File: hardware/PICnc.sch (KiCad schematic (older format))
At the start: 30 parts, among them P1 RPi GPIO, P2 STEP/DIR, P3 3.3v DIGITAL/ANALOG IO, P4 5v IO, P5 ICSP, P6 RPi GPIO, P7 5v RPi, P8 5v INP, U1 PIC32MX764F128H, U2 LP2985LV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

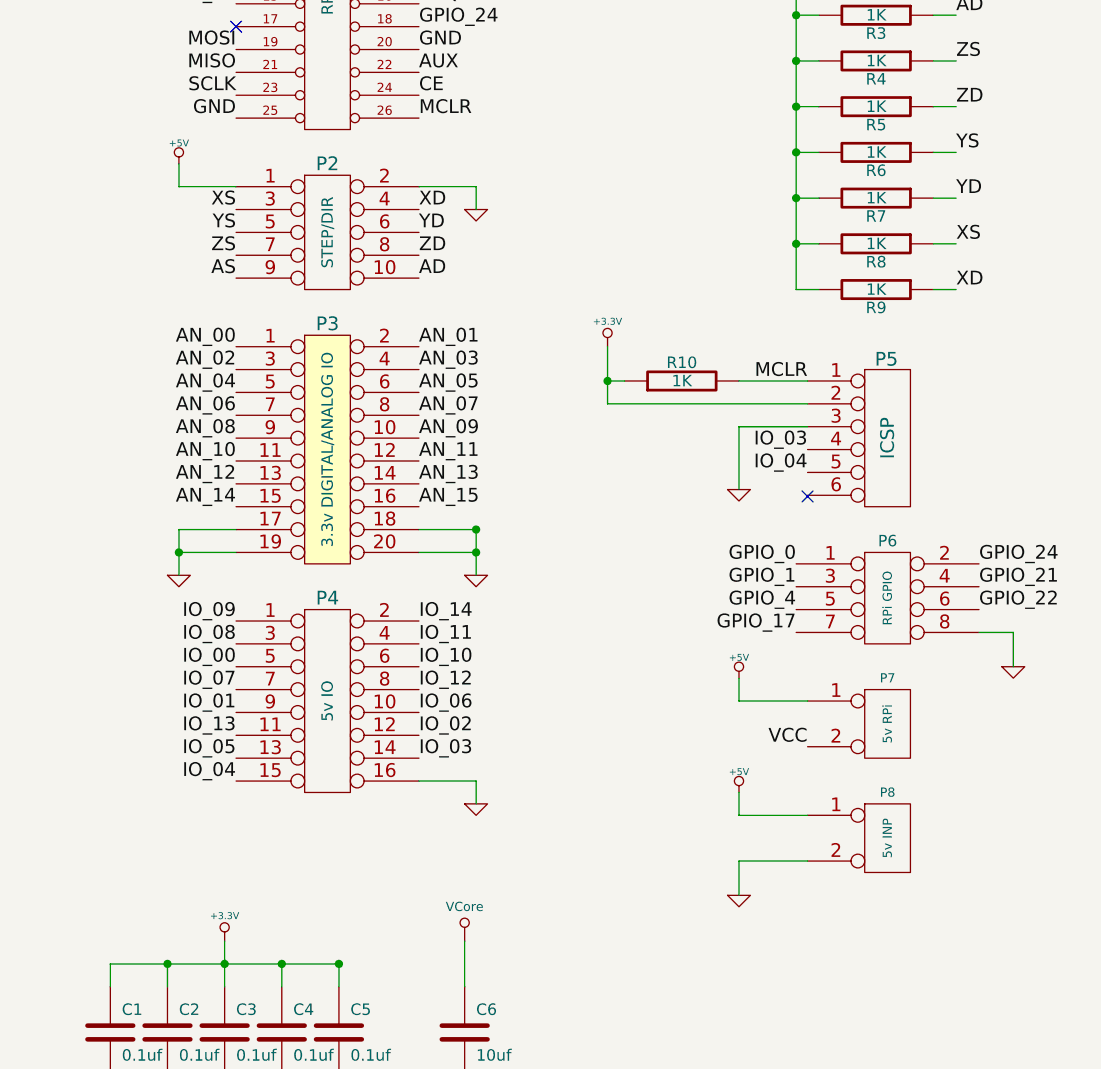
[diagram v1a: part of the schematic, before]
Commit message: fixed ICSP pinout
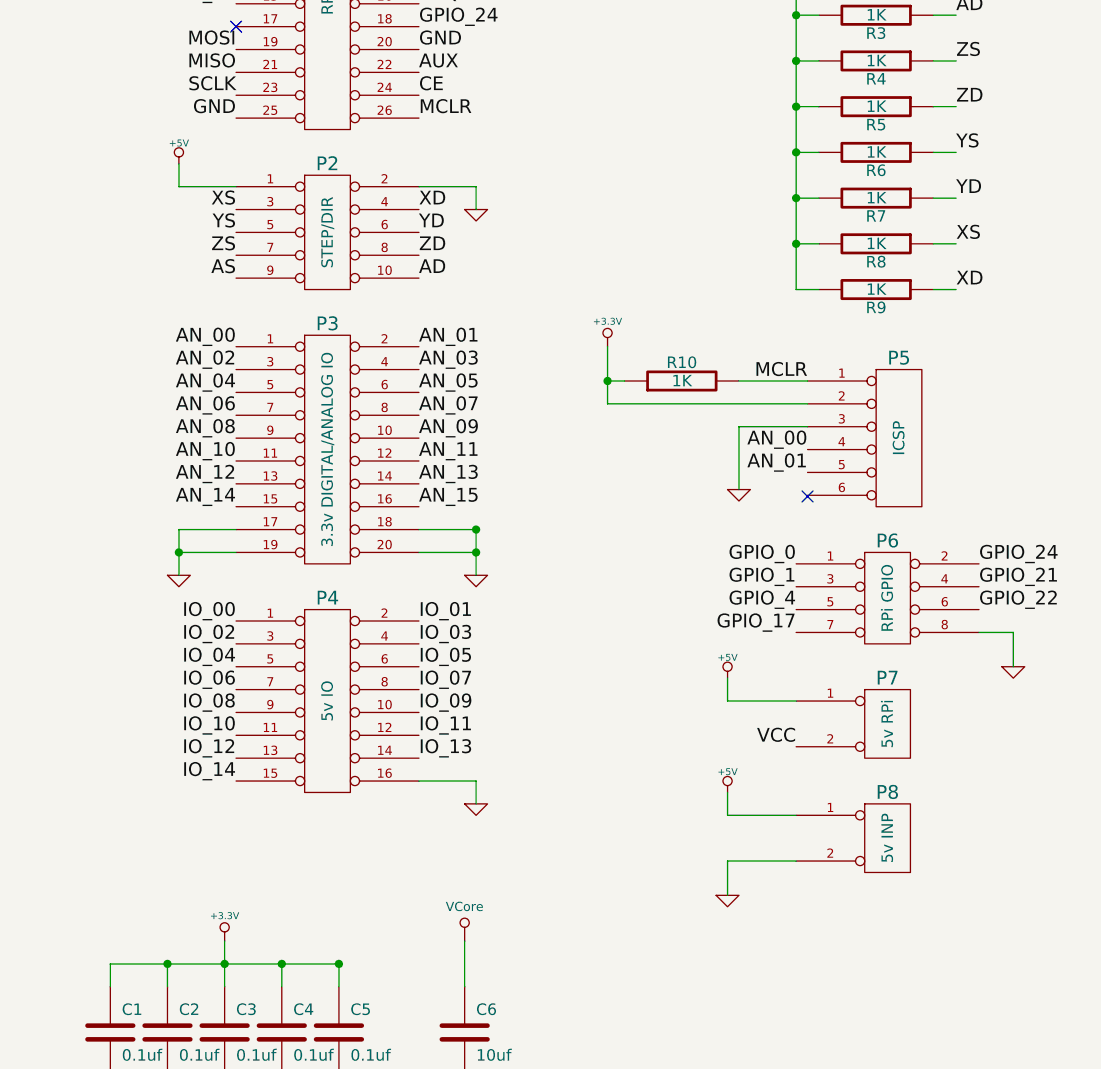
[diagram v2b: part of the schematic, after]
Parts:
- removed P2: STEP/DIR, symbol CONN_5X2
- removed P3: 3.3v DIGITAL/ANALOG IO, symbol CONN_10X2
- removed P4: 5v IO, symbol CONN_8X2
- removed P5: ICSP, symbol CONN_6
- removed P6: RPi GPIO, symbol CONN_4X2
- removed P7: 5v RPi, symbol CONN_2
- removed P8: 5v INP, symbol CONN_2
- added P2: STEP/DIR, symbol CON_5X2
- added P3: 3.3v DIGITAL/ANALOG IO, symbol CON_10X2
- added P4: 5v IO, symbol CON_8X2
- added P5: ICSP, symbol CON_6
- added P6: RPi GPIO, symbol CON_4X2
- added P7: 5v RPi, symbol CON_2
- added P8: 5v INP, symbol CON_2
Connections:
- net +3.3V: now also P5.2 (P2)
- net +5V: now also P2.1 (P1), P7.1 (P1), P8.1 (P1)
- net AD: now also P2.10 (P10)
- net AN_00: now also P3.1 (P1), P5.4 (P4)
- net AN_01: now also P3.2 (P2), P5.5 (P5)
- net AN_02: now also P3.3 (P3)
- net AN_03: now also P3.4 (P4)
- net AN_04: now also P3.5 (P5)
- net AN_05: now also P3.6 (P6)
- net AN_06: now also P3.7 (P7)
- net AN_07: now also P3.8 (P8)
- net AN_08: now also P3.9 (P9)
- net AN_09: now also P3.10 (P10)
- net AN_10: now also P3.11 (P11)
- net AN_11: now also P3.12 (P12)
- net AN_12: now also P3.13 (P13)
- net AN_13: now also P3.14 (P14)
- net AN_14: now also P3.15 (P15)
- net AN_15: now also P3.16 (P16)
- net AS: now also P2.9 (P9)
- net GND: now also P2.2 (P2), P3.17 (P17), P3.18 (P18), P3.19 (P19), P3.20 (P20), P4.16 (P16), P5.3 (P3), P6.8 (P8), P8.2 (P2)
- net GPIO_0: now also P6.1 (P1)
- net GPIO_1: now also P6.3 (P3)
- net GPIO_17: now also P6.7 (P7)
- net GPIO_21: now also P6.4 (P4)
- net GPIO_22: now also P6.6 (P6)
- net GPIO_24: now also P6.2 (P2)
- net GPIO_4: now also P6.5 (P5)
- net IO_00: now also P4.1 (P1)
- net IO_01: now also P4.2 (P2)
- net IO_02: now also P4.3 (P3)
- net IO_03: now also P4.4 (P4)
- net IO_04: now also P4.5 (P5)
- net IO_05: now also P4.6 (P6)
- net IO_06: now also P4.7 (P7)
- net IO_07: now also P4.8 (P8)
- net IO_08: now also P4.9 (P9)
- net IO_09: now also P4.10 (P10)
- net IO_10: now also P4.11 (P11)
- net IO_11: now also P4.12 (P12)
- net IO_12: now also P4.13 (P13)
- net IO_13: now also P4.14 (P14)
- net IO_14: now also P4.15 (P15)
- net MCLR: now also P5.1 (P1)
- net VCC: now also P7.2 (P2)
- net XD: now also P2.4 (P4)
- net XS: now also P2.3 (P3)
- net YD: now also P2.6 (P6)
- net YS: now also P2.5 (P5)
- net ZD: now also P2.8 (P8)
- net ZS: now also P2.7 (P7)
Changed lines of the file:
@@
-EESchema Schematic File Version 2  date Monday 18,February,2013 08:21:33 AM SGT
+EESchema Schematic File Version 2  date Monday 18,February,2013 12:46:50 PM SGT
 LIBS:power
 LIBS:device
@@
 Comment4 ""
 $EndDescr
-Wire Wire Line
-	9100 5850 9100 5700
-Wire Wire Line
-	9400 5500 9100 5500
-Wire Wire Line
-	9100 5500 9100 5400
+$Comp
+L CON_6 P5
+U 1 1 51218386
+P 9800 3850
+F 0 "P5" H 9800 4200 60  0000 C CNN
+F 1 "ICSP" V 9800 3850 50  0000 C CNN
+	1    9800 3850
+	1    0    0    -1
+$EndComp
+$Comp
+L CON_2 P8
+U 1 1 5121827C
+P 9750 5600
+F 0 "P8" H 9750 5800 60  0000 C CNN
+F 1 "5v INP" V 9750 5600 50  0000 C CNN
+	1    9750 5600
+	1    0    0    -1
+$EndComp
+$Comp
+L CON_2 P7
+U 1 1 51218259
+P 9750 5100
+F 0 "P7" H 9750 5300 60  0000 C CNN
+F 1 "5v RPi" V 9750 5100 50  0000 C CNN
+	1    9750 5100
+	1    0    0    -1
+$EndComp
+$Comp
+L CON_4X2 P6
+U 1 1 51218155
+P 9750 4550
+F 0 "P6" H 9750 4800 60  0000 C CNN
+F 1 "RPi GPIO" V 9750 4550 50  0000 C CNN
+	1    9750 4550
+	1    0    0    -1
+$EndComp
+$Comp
+L CON_5X2 P2
+U 1 1 51218129
+P 7300 2950
+F 0 "P2" H 7300 3250 60  0000 C CNN
+F 1 "STEP/DIR" V 7300 2950 50  0000 C CNN
+	1    7300 2950
+	1    0    0    -1
+$EndComp
+$Comp
+L CON_10X2 P3
+U 1 1 512180BA
+P 7300 3900
+F 0 "P3" H 7300 4450 60  0000 C CNN
+F 1 "3.3v DIGITAL/ANALOG IO" V 7300 3900 50  0000 C CNN
+	1    7300 3900
+	1    0    0    -1
+$EndComp
+$Comp
+L CON_8X2 P4
+U 1 1 51218077
+P 7300 5000
+F 0 "P4" H 7300 5450 60  0000 C CNN
+F 1 "5v IO" V 7300 5000 50  0000 C CNN
+	1    7300 5000
+	1    0    0    -1
+$EndComp
+Wire Wire Line
+	9050 5850 9050 5700
+Wire Wire Line
+	9350 5500 9050 5500
+Wire Wire Line
+	9050 5500 9050 5400
 Wire Wire Line
 	10300 4850 10300 4700
@@
 	7350 6750 6350 6750
 Wire Wire Line
-	9100 4900 9100 5000
-Wire Wire Line
-	9100 5000 9400 5000
+	9050 4900 9050 5000
+Wire Wire Line
+	9050 5000 9350 5000
 Wire Wire Line
 	7800 1350 7800 1250
 Wire Wire Line
-	9100 5700 9400 5700
+	9050 5700 9350 5700
 $Comp
 L GND #PWR01
 U 1 1 512070BF
-P 9100 5850
-F 0 "#PWR01" H 9100 5850 30  0001 C CNN
-F 1 "GND" H 9100 5780 30  0001 C CNN
-	1    9100 5850
-	1    0    0    -1
-$EndComp
-$Comp
-L CONN_2 P8
-U 1 1 512070B5
-P 9750 5600
-F 0 "P8" H 9750 5800 40  0000 C CNN
-F 1 "5v INP" V 9750 5600 40  0000 C CNN
-	1    9750 5600
+P 9050 5850
+F 0 "#PWR01" H 9050 5850 30  0001 C CNN
+F 1 "GND" H 9050 5780 30  0001 C CNN
+	1    9050 5850
 	1    0    0    -1
 $EndComp
@@
 L +5V #PWR02
 U 1 1 512070B4
-P 9100 5400
-F 0 "#PWR02" H 9100 5490 20  0001 C CNN
-F 1 "+5V" H 9100 5490 30  0000 C CNN
-	1    9100 5400
+P 9050 5400
+F 0 "#PWR02" H 9050 5490 20  0001 C CNN
+F 1 "+5V" H 9050 5490 30  0000 C CNN
+	1    9050 5400
 	1    0    0    -1
 $EndComp
@@
 Text Label 7900 1250 0    60   ~ 0
 VCC
-Text Label 9400 5200 2    60   ~ 0
+Text Label 9350 5200 2    60   ~ 0
 VCC
 $Comp
@@
 L +5V #PWR04
 U 1 1 512030D0
-P 9100 4900
-F 0 "#PWR04" H 9100 4990 20  0001 C CNN
-F 1 "+5V" H 9100 4990 30  0000 C CNN
-	1    9100 4900
-	1    0    0    -1
-$EndComp
-$Comp
-L CONN_2 P7
-U 1 1 51203037
-P 9750 5100
-F 0 "P7" H 9750 5300 40  0000 C CNN
-F 1 "5v RPi" V 9750 5100 40  0000 C CNN
-	1    9750 5100
-	1    0    0    -1
-$EndComp
-$Comp
-L CONN_4X2 P6
-U 1 1 51203010
-P 9750 4550
-F 0 "P6" H 9750 4800 50  0000 C CNN
-F 1 "RPi GPIO" V 9750 4550 40  0000 C CNN
-	1    9750 4550
+P 9050 4900
+F 0 "#PWR04" H 9050 4990 20  0001 C CNN
+F 1 "+5V" H 9050 4990 30  0000 C CNN
+	1    9050 4900
 	1    0    0    -1
 $EndComp
@@
 Text Label 5150 2650 0    60   ~ 0
 AS
-$Comp
-L CONN_8X2 P4
-U 1 1 511F63B8
-P 7300 5000
-F 0 "P4" H 7300 5450 60  0000 C CNN
-F 1 "5v IO" V 7300 5000 50  0000 C CNN
-	1    7300 5000
-	1    0    0    -1
-$EndComp
 Text Label 6900 1950 2    60   ~ 0
 GPIO_22
@@
 Text Label 5150 4550 0    60   ~ 0
 MOSI
-$Comp
-L CONN_10X2 P3
-U 1 1 5119C222
-P 7300 3900
-F 0 "P3" H 7300 4450 60  0000 C CNN
-F 1 "3.3v DIGITAL/ANALOG IO" V 7300 3900 50  0000 C CNN
-	1    7300 3900
-	1    0    0    -1
-$EndComp
 Text Label 7700 1950 0    60   ~ 0
 REQ
@@
 GND
 $Comp
-L CONN_5X2 P2
-U 1 1 51139363
-P 7300 2950
-F 0 "P2" H 7300 3250 60  0000 C CNN
-F 1 "STEP/DIR" V 7300 2950 50  0000 C CNN
-	1    7300 2950
-	1    0    0    -1
-$EndComp
-$Comp
 L CONN_13X2 P1
 U 1 1 511392E7
@@
 NoConn ~ 5150 3450
 NoConn ~ 9400 4105
-$Comp
-L CONN_6 P5
-U 1 1 50057C6F
-P 9750 3850
-F 0 "P5" H 9745 4195 60  0000 C CNN
-F 1 "ICSP" V 9750 3850 60  0000 C CNN
-	1    9750 3850
-	1    0    0    -1
-$EndComp
 Text Label 10050 2200 0    60   ~ 0
 ZS
@@
 $EndComp
 NoConn ~ 3900 6500
+Text Label 7700 5250 0    60   ~ 0
+IO_13
+Text Label 7700 5150 0    60   ~ 0
+IO_11
+Text Label 6900 4950 2    60   ~ 0
+IO_06
+Text Label 7700 4950 0    60   ~ 0
+IO_07
+Text Label 7700 4850 0    60   ~ 0
+IO_05
+Text Label 7700 4750 0    60   ~ 0
+IO_03
+Text Label 7700 4650 0    60   ~ 0
+IO_01
+Text Label 6900 5350 2    60   ~ 0
+IO_14
+Text Label 6900 5250 2    60   ~ 0
+IO_12
 Text Label 6900 5150 2    60   ~ 0
-IO_13
-Text Label 7700 4750 0    60   ~ 0
-IO_11
+IO_10
+Text Label 6900 5050 2    60   ~ 0
+IO_08
 Text Label 7700 5050 0    60   ~ 0
-IO_06
-Text Label 6900 4950 2    60   ~ 0
-IO_07
-Text Label 6900 5250 2    60   ~ 0
-IO_05
-Text Label 7700 5250 0    60   ~ 0
-IO_03
-Text Label 6900 5050 2    60   ~ 0
-IO_01
-Text Label 7700 4650 0    60   ~ 0
-IO_14
-Text Label 7700 4950 0    60   ~ 0
-IO_12
-Text Label 7700 4850 0    60   ~ 0
-IO_10
+IO_09
+Text Label 6900 4850 2    60   ~ 0
+IO_04
 Text Label 6900 4750 2    60   ~ 0
-IO_08
+IO_02
 Text Label 6900 4650 2    60   ~ 0
-IO_09
-Text Label 6900 5350 2    60   ~ 0
-IO_04
-Text Label 7700 5150 0    60   ~ 0
-IO_02
-Text Label 6900 4850 2    60   ~ 0
 IO_00
 $Comp
@@
 $EndComp
 Text Label 9400 4000 2    60   ~ 0
-IO_04
+AN_01
 Text Label 9400 3900 2    60   ~ 0
-IO_03
+AN_00
 $Comp
 L +3.3V #PWR015

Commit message: added BOM
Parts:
- C1, C2, C3, C4, C5: footprint (none) -> SM0402; Element14 Order Code (none) -> 1833861; Mftr. & Part No. (none) -> AVX - 0402YC104KAT2A
- C6, C8: footprint (none) -> SM0603; Element14 Order Code (none) -> 1867954; Mftr. & Part No. (none) -> AVX - 0603ZD106MAT2A
- C7: footprint (none) -> SM0603; Element14 Order Code (none) -> 1844259; Mftr. & Part No. (none) -> TDK - C1608Y5V1A225Z
- D1: footprint (none) -> LED-0603; Element14 Order Code (none) -> 1226390; Mftr. & Part No. (none) -> OSRAM - LSQ976-Z
- R1, R10: footprint (none) -> SM0402; Element14 Order Code (none) -> 195030; Mftr. & Part No. (none) -> YAGEO (PHYCOMP) - 2322 705 70102
- R2, R3, R4, R5, R6, R7, R8, R9: value 1K -> 2K2; footprint (none) -> SM0402; Element14 Order Code (none) -> 1174156; Mftr. & Part No. (none) -> TE CONNECTIVITY / NEOHM - CRG0402J2K2
- U1: Element14 Order Code (none) -> 1971889; Mftr. & Part No. (none) -> MICROCHIP - PIC32MX764F128H-I/PT
- U2: footprint (none) -> SOT23-5; Element14 Order Code (none) -> 2126531; Mftr. & Part No. (none) -> TEXAS INSTRUMENTS - LP2985-33DBVR
- X1: Element14 Order Code (none) -> 1170435; Mftr. & Part No. (none) -> MURATA - CSTCC8M00G53-R0
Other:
- moved on the sheet: C7
